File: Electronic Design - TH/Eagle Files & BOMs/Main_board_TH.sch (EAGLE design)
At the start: 57 parts, among them M1 ARDUINO-NANO-3.0, Q1 IRF9520, Q2 IRF9520

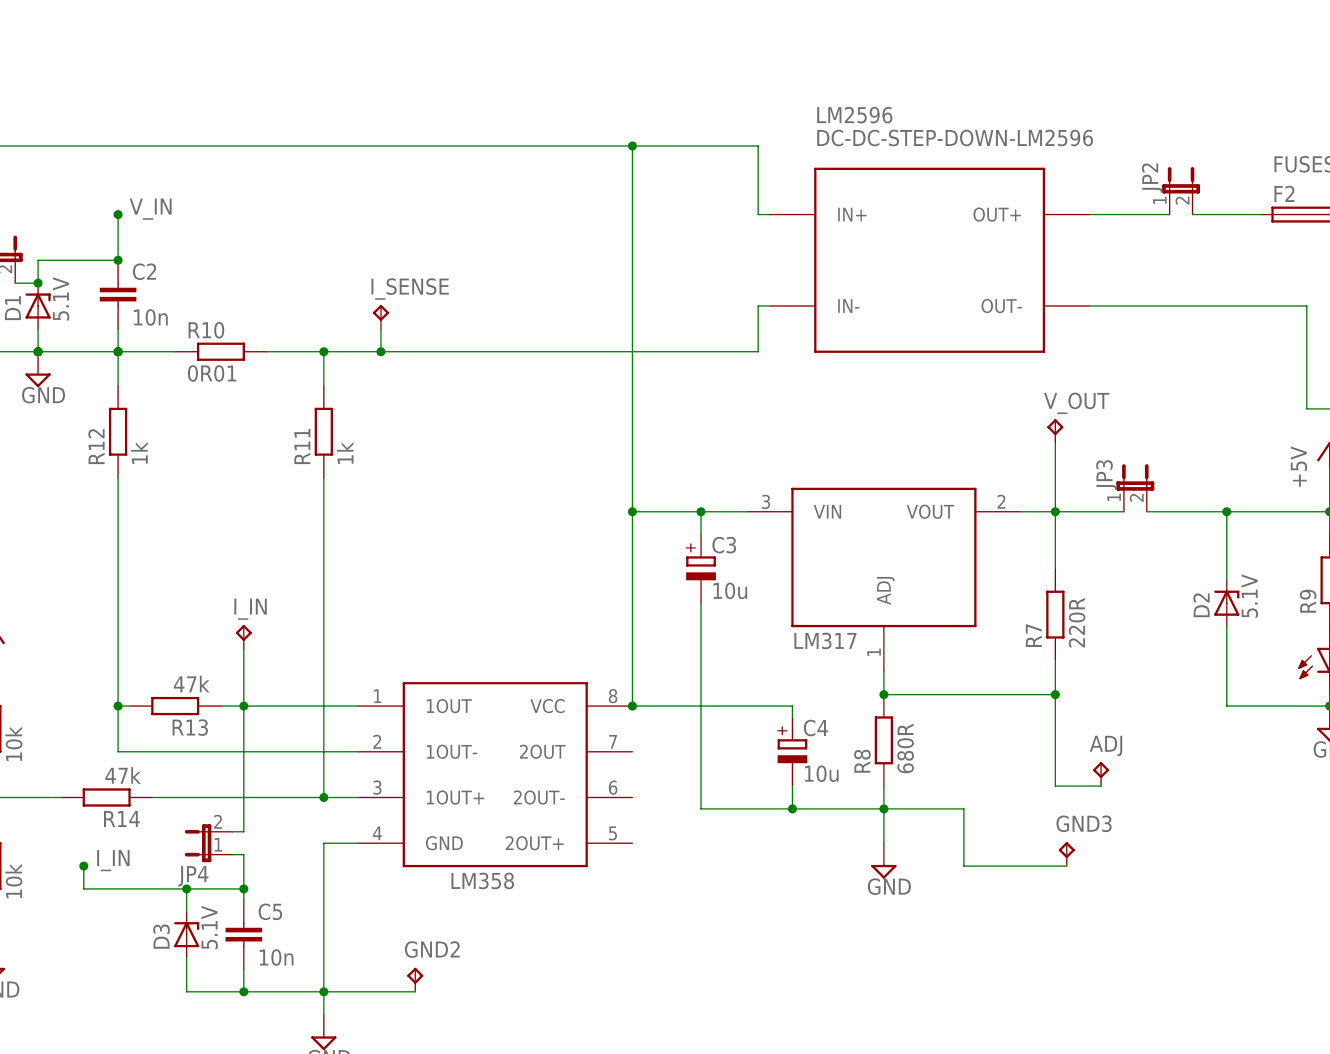
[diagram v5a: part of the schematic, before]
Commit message: neraming jumpers, changing hole size of r10 and monor adjustments to underside of PCB
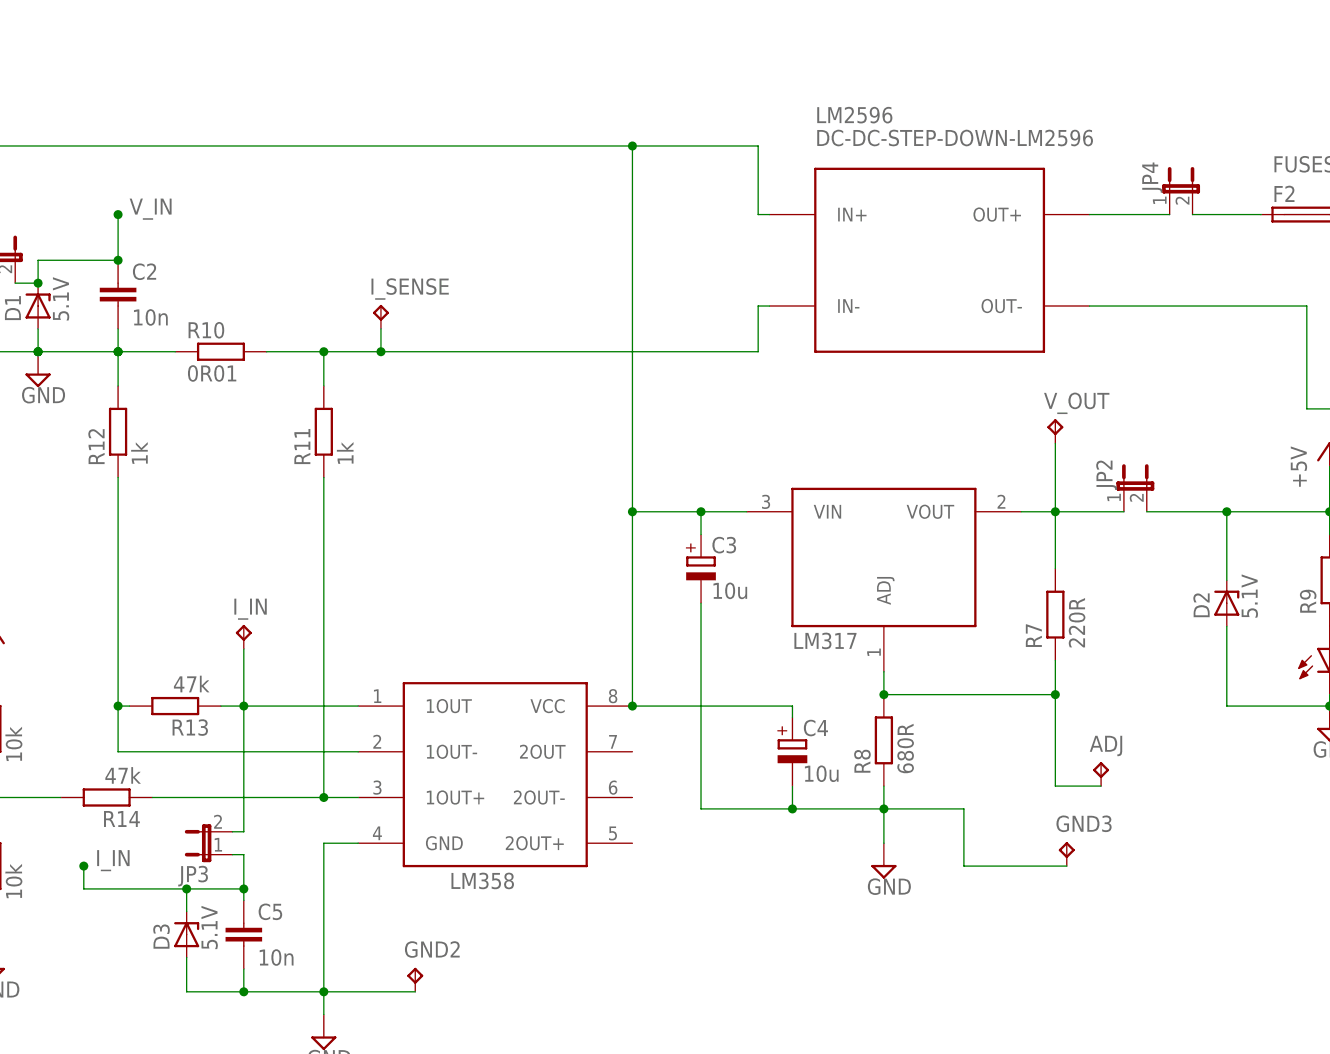
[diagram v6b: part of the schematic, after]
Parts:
- R10: device resistor:R-EU_0207/15 -> resistor:R-EU_0613/15
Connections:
- net +5V: now also JP2.2; no longer JP3.2
- net I_IN: now also JP3.1; no longer JP4.1
- net I_IN_PRE: now also JP3.2; no longer JP4.2
- net N$15: now also JP4.1; no longer JP2.1
- net N$16: now also JP4.2; no longer JP2.2
- net N$18: now also JP2.1; no longer JP3.1
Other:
- moved on the sheet: JP2, JP3, JP4
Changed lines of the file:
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@@
 <part name="SCREEN_OUT" library="pinhead" deviceset="PINHD-1X4" device=""/>
 <part name="+5V4" library="supply1" deviceset="+5V" device=""/>
-<part name="R10" library="resistor" deviceset="R-EU_" device="0207/15" value="0R01"/>
+<part name="R10" library="resistor" deviceset="R-EU_" device="0613/15" value="0R01"/>
 <part name="SUPPLY8" library="supply2" deviceset="GND" device=""/>
 <part name="R7" library="resistor" deviceset="R-EU_" device="0207/10" value="220R"/>
@@
 <part name="I_SENSE" library="testpad" deviceset="TP" device="PAD1-13" value="TPPAD1-13"/>
 <part name="I_IN" library="testpad" deviceset="TP" device="PAD1-13" value="TPPAD1-13"/>
+<part name="JP4" library="jumper" deviceset="JP1E" device=""/>
 <part name="JP2" library="jumper" deviceset="JP1E" device=""/>
+<part name="GND2" library="testpad" deviceset="TP" device="PAD1-13" value="TPPAD1-13"/>
 <part name="JP3" library="jumper" deviceset="JP1E" device=""/>
-<part name="GND2" library="testpad" deviceset="TP" device="PAD1-13" value="TPPAD1-13"/>
-<part name="JP4" library="jumper" deviceset="JP1E" device=""/>
 <part name="SUPPLY3" library="supply2" deviceset="GND" device=""/>
 <part name="V_OUT" library="testpad" deviceset="TP" device="PAD1-13" value="TPPAD1-13"/>
@@
 <instance part="I_SENSE" gate="G$1" x="40.64" y="71.12"/>
 <instance part="I_IN" gate="G$1" x="25.4" y="35.56"/>
-<instance part="JP2" gate="A" x="128.27" y="83.82"/>
-<instance part="JP3" gate="A" x="123.19" y="50.8"/>
+<instance part="JP4" gate="A" x="128.27" y="83.82"/>
+<instance part="JP2" gate="A" x="123.19" y="50.8"/>
 <instance part="GND2" gate="G$1" x="44.45" y="-2.54"/>
-<instance part="JP4" gate="A" x="21.59" y="10.16" rot="R90"/>
+<instance part="JP3" gate="A" x="21.59" y="10.16" rot="R90"/>
 <instance part="SUPPLY3" gate="GND" x="-113.03" y="26.67"/>
 <instance part="V_OUT" gate="G$1" x="115.57" y="58.42"/>
@@
 <pinref part="R9" gate="G$1" pin="2"/>
 <wire x1="146.05" y1="48.26" x2="146.05" y2="45.72" width="0.1524" layer="91"/>
-<pinref part="JP3" gate="A" pin="2"/>
+<pinref part="JP2" gate="A" pin="2"/>
 <wire x1="125.73" y1="48.26" x2="134.62" y2="48.26" width="0.1524" layer="91"/>
 <junction x="134.62" y="48.26"/>
@@
 <wire x1="25.4" y1="6.35" x2="19.05" y2="6.35" width="0.1524" layer="91"/>
 <wire x1="19.05" y1="6.35" x2="19.05" y2="3.81" width="0.1524" layer="91"/>
-<pinref part="JP4" gate="A" pin="1"/>
+<pinref part="JP3" gate="A" pin="1"/>
 <wire x1="24.13" y1="10.16" x2="25.4" y2="10.16" width="0.1524" layer="91"/>
 <wire x1="19.05" y1="6.35" x2="7.62" y2="6.35" width="0.1524" layer="91"/>
@@
 <net name="N$15" class="0">
 <segment>
-<pinref part="JP2" gate="A" pin="1"/>
+<pinref part="JP4" gate="A" pin="1"/>
 <pinref part="LM2596" gate="G$1" pin="OUT+"/>
 <wire x1="128.27" y1="81.28" x2="119.38" y2="81.28" width="0.1524" layer="91"/>
@@
 <net name="N$16" class="0">
 <segment>
-<pinref part="JP2" gate="A" pin="2"/>
+<pinref part="JP4" gate="A" pin="2"/>
 <pinref part="F2" gate="G$1" pin="1"/>
 <wire x1="130.81" y1="81.28" x2="138.43" y2="81.28" width="0.1524" layer="91"/>
@@
 <wire x1="115.57" y1="48.26" x2="111.76" y2="48.26" width="0.1524" layer="91"/>
 <wire x1="115.57" y1="48.26" x2="115.57" y2="41.91" width="0.1524" layer="91"/>
-<pinref part="JP3" gate="A" pin="1"/>
+<pinref part="JP2" gate="A" pin="1"/>
 <wire x1="115.57" y1="48.26" x2="123.19" y2="48.26" width="0.1524" layer="91"/>
 <junction x="115.57" y="48.26"/>
@@
 <junction x="25.4" y="26.67"/>
 <wire x1="25.4" y1="26.67" x2="25.4" y2="12.7" width="0.1524" layer="91"/>
-<pinref part="JP4" gate="A" pin="2"/>
+<pinref part="JP3" gate="A" pin="2"/>
 <wire x1="24.13" y1="12.7" x2="25.4" y2="12.7" width="0.1524" layer="91"/>
 <pinref part="I_IN" gate="G$1" pin="TP"/>
